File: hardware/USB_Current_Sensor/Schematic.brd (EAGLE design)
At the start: 37.8 x 22.9 mm, 8 parts, among them K1 629004113921, K2 62900416021, U1 INA139NA/250

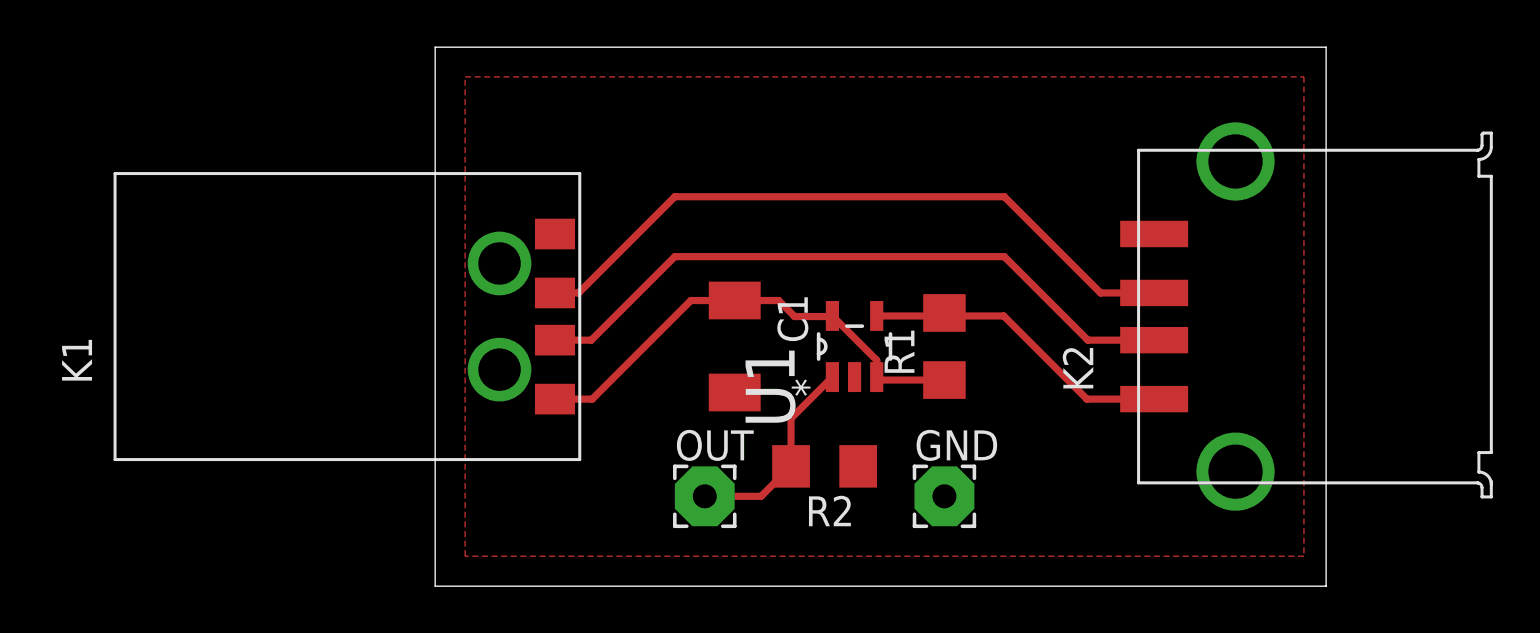
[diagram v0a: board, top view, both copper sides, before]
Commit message: PCB design for usb current monitor
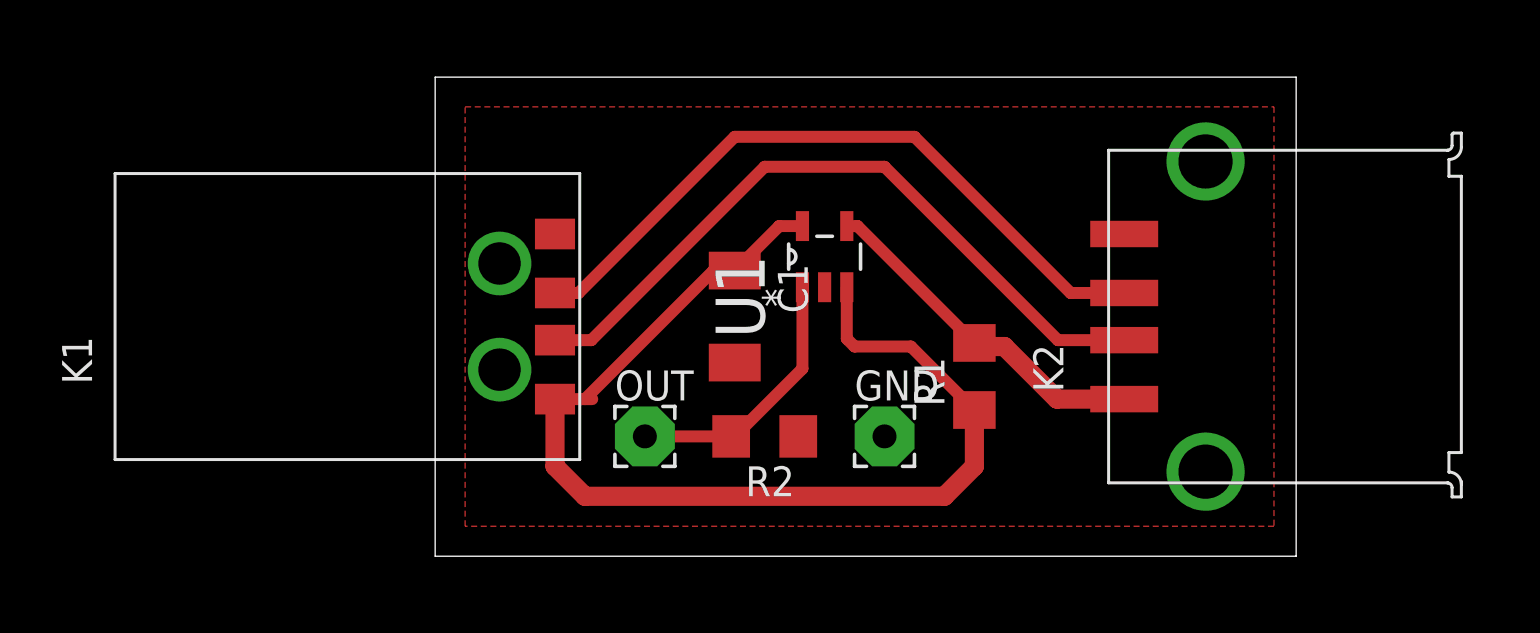
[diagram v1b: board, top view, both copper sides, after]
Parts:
- moved U1 4.02 mm to (19.1, 43.2)
- moved OUT 3.59 mm to (11.4, 35.6)
- moved GND 3.59 mm to (21.6, 35.6)
- moved R2 2.84 mm to (16.5, 35.6)
- moved R1 1.80 mm to (25.4, 38.1)
- moved C1 1.27 mm to (15.2, 40.6)
- moved K2 1.27 mm to (31.8, 40.6)
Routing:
- net N$4: track 20.1 -> 47.1 mm
- net N$5: track 8.69 -> 11.3 mm
- net N$3: track 28.3 -> 30.2 mm
- net N$6: track 13.4 -> 14.8 mm
- net N$2: track 28.8 -> 29.6 mm
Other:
- board size 37.8 x 22.9 mm -> 36.5 x 20.3 mm
